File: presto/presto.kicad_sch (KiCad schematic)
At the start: 1 part

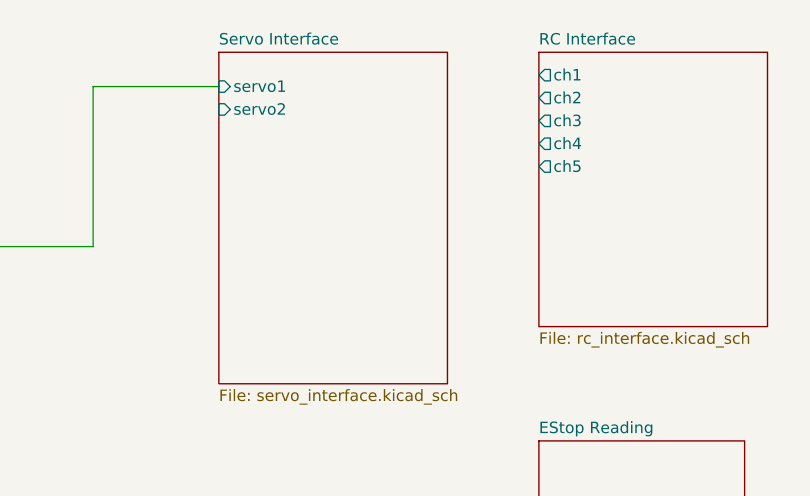
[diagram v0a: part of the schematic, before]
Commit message: RC and Servo interface schematic done
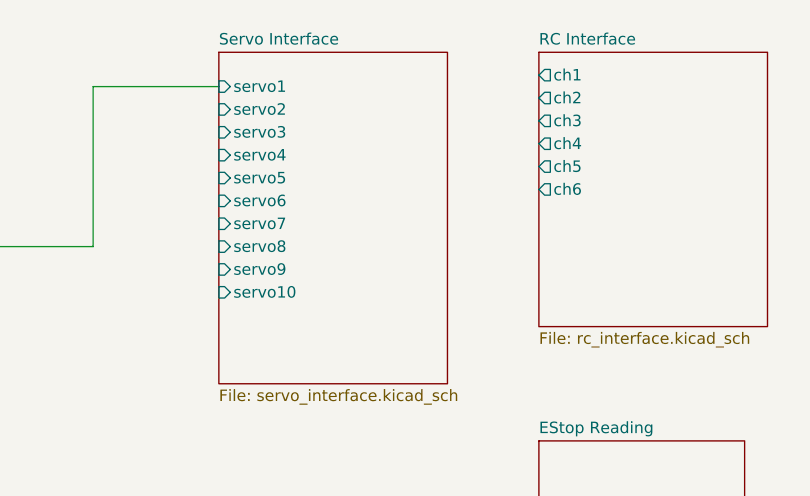
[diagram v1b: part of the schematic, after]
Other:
- sheet RC Interface ports: added ch6; removed none
- sheet Servo Interface ports: added servo10, servo3, servo4, servo5, servo6, servo7, servo8, servo9; removed none
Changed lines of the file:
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@@
+			)
+		)
+		(pin "ch6" output
+			(at 228.6 53.34 180)
+			(effects
+				(font
+					(size 1.27 1.27)
+				)
+				(justify left)
 			)
 		)
@@
 			(effects
 				(font
+					(size 1.27 1.27)
+				)
+				(justify left)
+			)
+		)
+		(pin "servo3" input
+			(at 193.04 46.99 180)
+			(effects
+				(font
+					(size 1.27 1.27)
+				)
+				(justify left)
+			)
+		)
+		(pin "servo4" input
+			(at 193.04 49.53 180)
+			(effects
+				(font
+					(size 1.27 1.27)
+				)
+				(justify left)
+			)
+		)
+		(pin "servo5" input
+			(at 193.04 52.07 180)
+			(effects
+				(font
+					(size 1.27 1.27)
+				)
+				(justify left)
+			)
+		)
+		(pin "servo6" input
+			(at 193.04 54.61 180)
+			(effects
+				(font
+					(size 1.27 1.27)
+				)
+				(justify left)
+			)
+		)
+		(pin "servo7" input
+			(at 193.04 57.15 180)
+			(effects
+				(font
+					(size 1.27 1.27)
+				)
+				(justify left)
+			)
+		)
+		(pin "servo8" input
+			(at 193.04 59.69 180)
+			(effects
+				(font
+					(size 1.27 1.27)
+				)
+				(justify left)
+			)
+		)
+		(pin "servo9" input
+			(at 193.04 62.23 180)
+			(effects
+				(font
+					(size 1.27 1.27)
+				)
+				(justify left)
+			)
+		)
+		(pin "servo10" input
+			(at 193.04 64.77 180)
+			(effects
+				(font

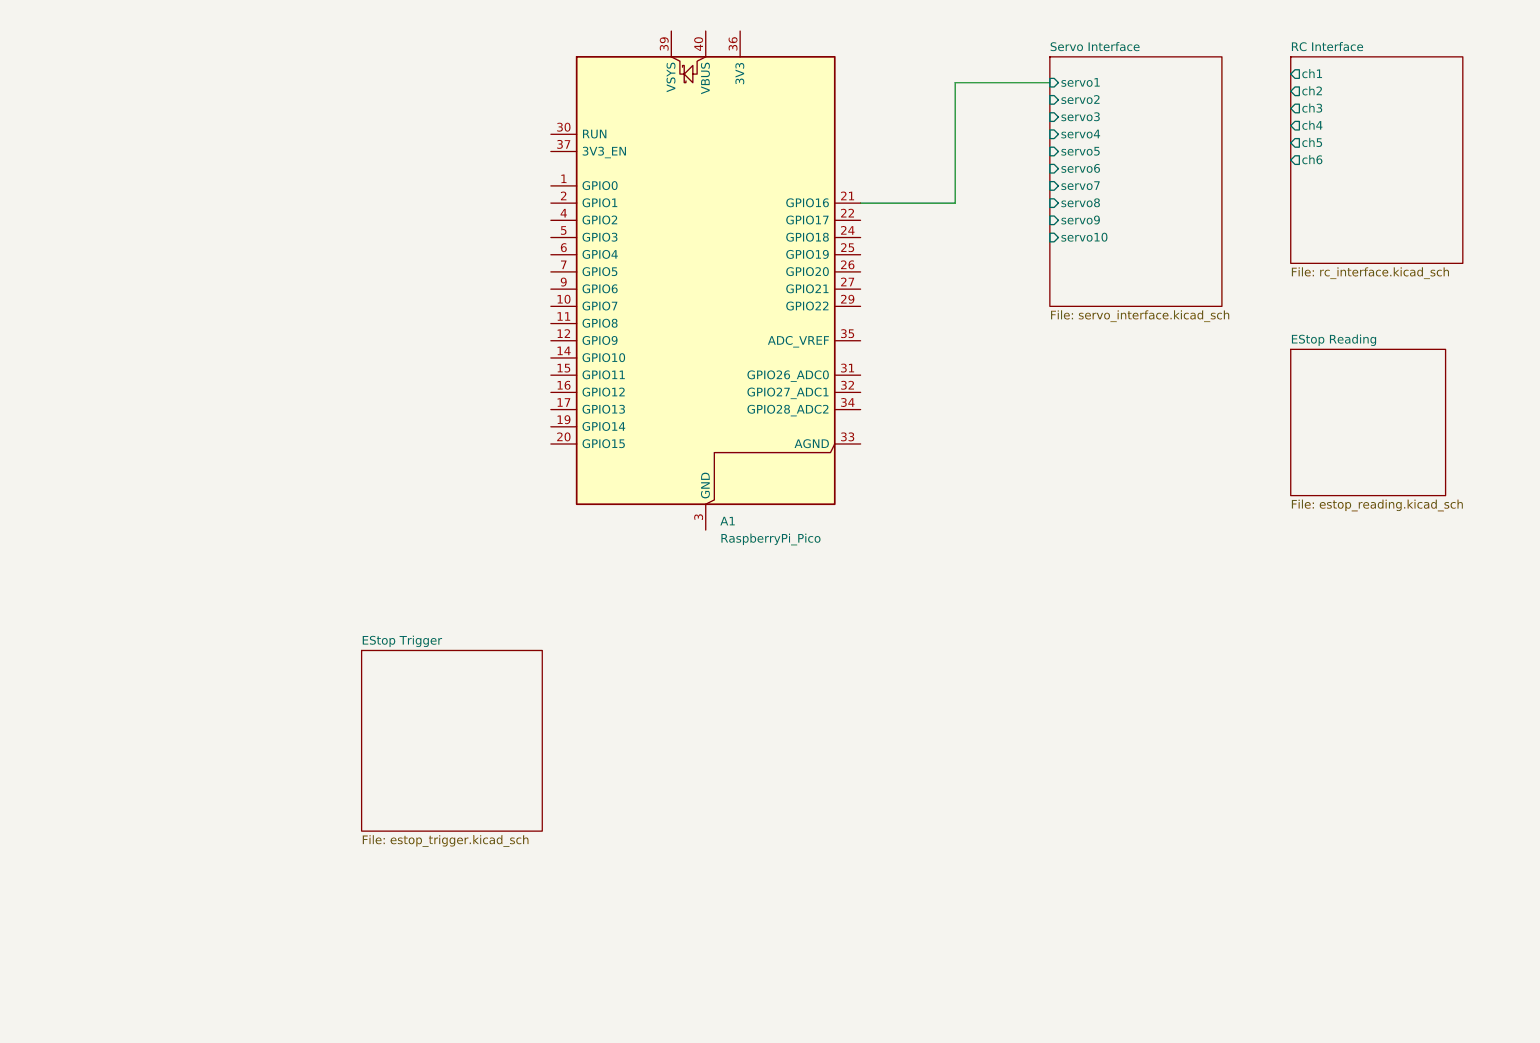
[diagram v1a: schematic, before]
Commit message: Added estop, power, led schematics
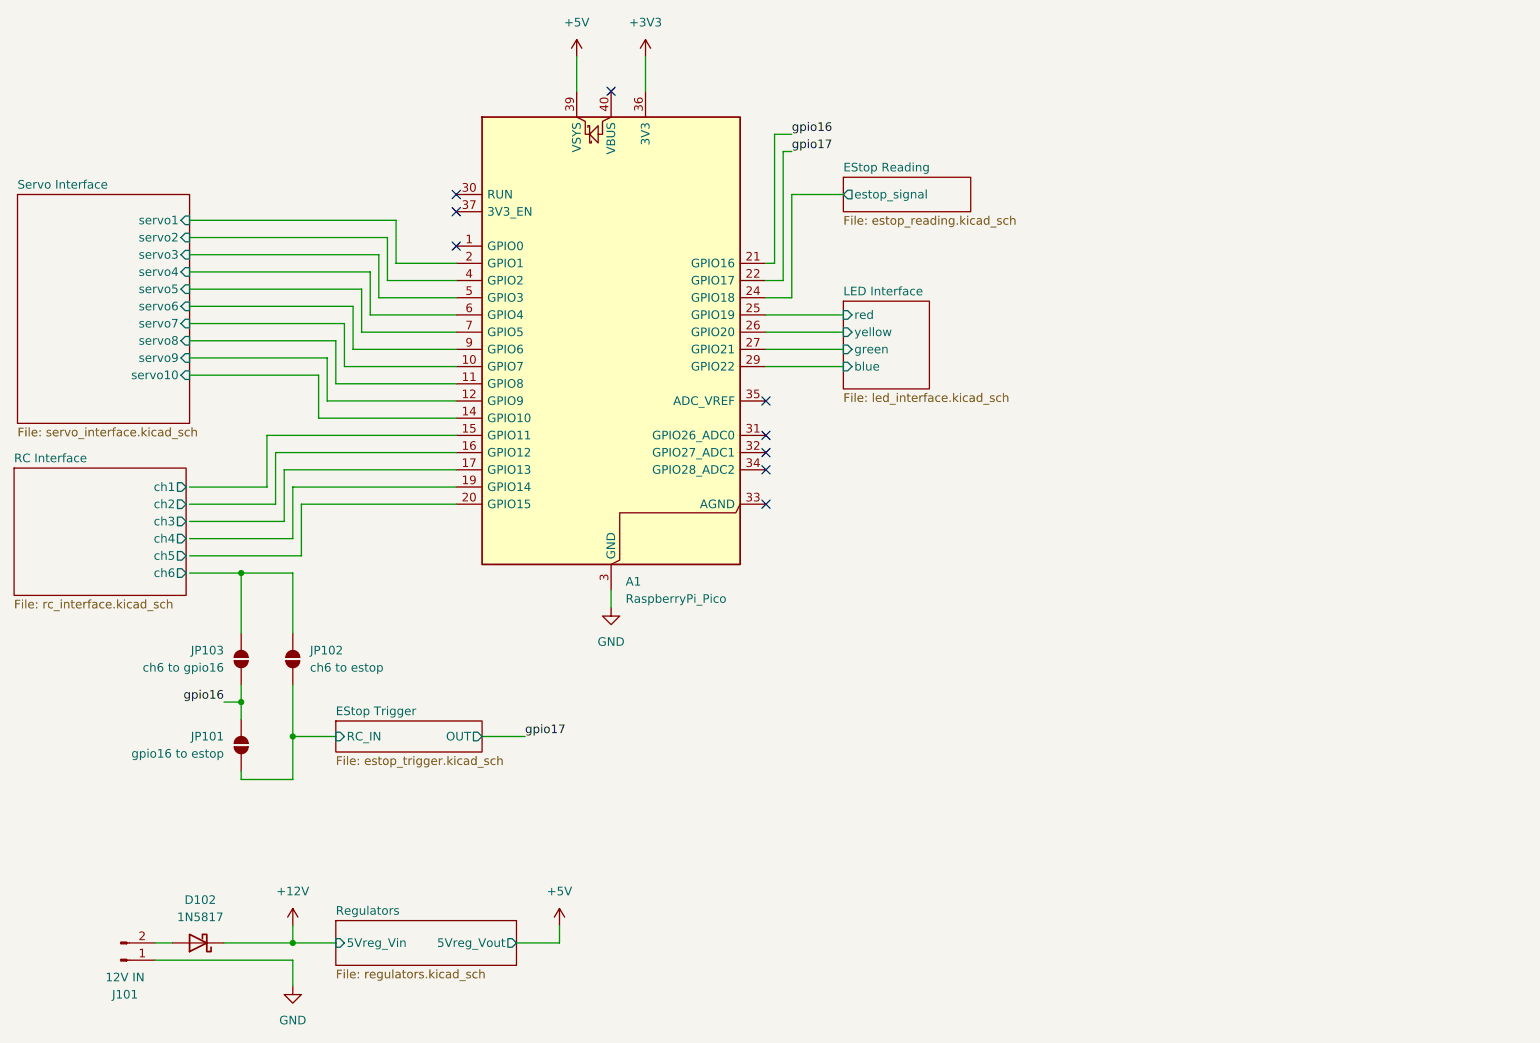
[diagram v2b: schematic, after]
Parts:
- added D102: 1N5817, Diode_THT:D_DO-41_SOD81_P10.16mm_Horizontal, symbol Diode:1N5817
- added J101: 12V IN, Connector_AMASS:AMASS_XT30PW-M_1x02_P2.50mm_Horizontal, symbol Connector:Conn_01x02_Pin
- added JP101: gpio16 to estop, Jumper:SolderJumper-2_P1.3mm_Open_RoundedPad1.0x1.5mm, symbol Jumper:SolderJumper_2_Open
- added JP102: ch6 to estop, Jumper:SolderJumper-2_P1.3mm_Open_RoundedPad1.0x1.5mm, symbol Jumper:SolderJumper_2_Open
- added JP103: ch6 to gpio16, Jumper:SolderJumper-2_P1.3mm_Open_RoundedPad1.0x1.5mm, symbol Jumper:SolderJumper_2_Open
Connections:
- net Servo Interface/servo1: now also A1.2 (GPIO1); no longer A1.21 (GPIO16)
- net Servo Interface/servo10: now also A1.14 (GPIO10)
- net Servo Interface/servo2: now also A1.4 (GPIO2)
- net Servo Interface/servo3: now also A1.5 (GPIO3)
- net Servo Interface/servo4: now also A1.6 (GPIO4)
- net Servo Interface/servo5: now also A1.7 (GPIO5)
- net Servo Interface/servo6: now also A1.9 (GPIO6)
- net Servo Interface/servo7: now also A1.10 (GPIO7)
- net Servo Interface/servo8: now also A1.11 (GPIO8)
- net Servo Interface/servo9: now also A1.12 (GPIO9)
- net GND: now reaches A1.13 (GND), A1.18 (GND), A1.23 (GND), A1.28 (GND), A1.3 (GND), A1.38 (GND), A1.8 (GND)
- net GND: now also J101.1 (Pin_1)
- net gpio17: now reaches A1.22 (GPIO17)
- net EStop Reading/estop_signal: now reaches A1.24 (GPIO18)
- net LED Interface/red: now reaches A1.25 (GPIO19)
- net LED Interface/yellow: now reaches A1.26 (GPIO20)
- net LED Interface/green: now reaches A1.27 (GPIO21)
- net LED Interface/blue: now reaches A1.29 (GPIO22)
- net +3V3: now reaches A1.36 (3V3)
- net +5V: now reaches A1.39 (VSYS)
- new net: JP102.1 (A), JP103.1 (A)
- new net: D102.2 (A), J101.2 (Pin_2)
- new net +12V: D102.1 (K)
- new net EStop Trigger/RC_IN: JP101.2 (B), JP102.2 (B)
- new net gpio16: A1.21 (GPIO16), JP101.1 (A), JP103.2 (B)
- no-connect marks 0 -> 9
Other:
- added sheet LED Interface (led_interface.kicad_sch)
- added sheet Regulators (regulators.kicad_sch)
- sheet EStop Reading ports: added estop_signal; removed none
- sheet EStop Trigger ports: added OUT, RC_IN; removed none
- moved on the sheet: A1

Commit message: Presto PCB edited with schematic, components placed, wiring in progress
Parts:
- renumbered A1 to A101, D102 to D101, JP103 to JP101, JP101 to JP102, JP102 to JP103
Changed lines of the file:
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@@
 		(on_board yes)
 		(dnp no)
-		(property "Reference" "JP102"
+		(property "Reference" "JP103"
 			(at 83.82 125.7299 90)
 			(effects
@@
 			(project ""
 				(path "/0fac30c0-3f82-4ab4-8888-b9c60b2e0ca9"
-					(reference "JP102")
+					(reference "JP103")
 					(unit 1)
 				)
@@
 		(dnp no)
 		(fields_autoplaced yes)
-		(property "Reference" "A1"
+		(property "Reference" "A101"
 			(at 130.4133 115.57 0)
 			(effects
@@
 			(project ""
 				(path "/0fac30c0-3f82-4ab4-8888-b9c60b2e0ca9"
-					(reference "A1")
+					(reference "A101")
 					(unit 1)
 				)
@@
 		(on_board yes)
 		(dnp no)
-		(property "Reference" "JP101"
+		(property "Reference" "JP102"
 			(at 71.12 138.4299 90)
 			(effects
@@
 			(project "presto"
 				(path "/0fac30c0-3f82-4ab4-8888-b9c60b2e0ca9"
-					(reference "JP101")
+					(reference "JP102")
 					(unit 1)
 				)
@@
 		(dnp no)
 		(fields_autoplaced yes)
-		(property "Reference" "#PWR0104"
+		(property "Reference" "#PWR0101"
 			(at 81.28 170.18 0)
 			(effects
@@
 			(project "presto"
 				(path "/0fac30c0-3f82-4ab4-8888-b9c60b2e0ca9"
-					(reference "#PWR0104")
+					(reference "#PWR0101")
 					(unit 1)
 				)
@@
 		(dnp no)
 		(fields_autoplaced yes)
-		(property "Reference" "D102"
+		(property "Reference" "D101"
 			(at 67.6275 162.56 0)
 			(effects
@@
 			(project ""
 				(path "/0fac30c0-3f82-4ab4-8888-b9c60b2e0ca9"
-					(reference "D102")
+					(reference "D101")
 					(unit 1)
 				)
@@
 		(dnp no)
 		(fields_autoplaced yes)
-		(property "Reference" "#PWR0102"
+		(property "Reference" "#PWR0105"
 			(at 128.27 125.73 0)
 			(effects
@@
 			(project "presto"
 				(path "/0fac30c0-3f82-4ab4-8888-b9c60b2e0ca9"
-					(reference "#PWR0102")
+					(reference "#PWR0105")
 					(unit 1)
 				)
@@
 		(dnp no)
 		(fields_autoplaced yes)
-		(property "Reference" "#PWR0103"
+		(property "Reference" "#PWR0102"
 			(at 81.28 181.61 0)
 			(effects
@@
 			(project "presto"
 				(path "/0fac30c0-3f82-4ab4-8888-b9c60b2e0ca9"
-					(reference "#PWR0103")
+					(reference "#PWR0102")
 					(unit 1)
 				)
@@
 		(dnp no)
 		(fields_autoplaced yes)
-		(property "Reference" "#PWR0106"
+		(property "Reference" "#PWR0104"
 			(at 123.19 41.91 0)
 			(effects
@@
 			(project "presto"
 				(path "/0fac30c0-3f82-4ab4-8888-b9c60b2e0ca9"
-					(reference "#PWR0106")
+					(reference "#PWR0104")
 					(unit 1)
 				)
@@
 		(dnp no)
 		(fields_autoplaced yes)
-		(property "Reference" "#PWR0101"
+		(property "Reference" "#PWR0106"
 			(at 133.35 41.91 0)
 			(effects
@@
 			(project "presto"
 				(path "/0fac30c0-3f82-4ab4-8888-b9c60b2e0ca9"
-					(reference "#PWR0101")
+					(reference "#PWR0106")
 					(unit 1)
 				)
@@
 		(dnp no)
 		(fields_autoplaced yes)
-		(property "Reference" "#PWR0105"
+		(property "Reference" "#PWR0103"
 			(at 120.65 170.18 0)
 			(effects
@@
 			(project "presto"
 				(path "/0fac30c0-3f82-4ab4-8888-b9c60b2e0ca9"
-					(reference "#PWR0105")
+					(reference "#PWR0103")
 					(unit 1)
 				)
@@
 		(on_board yes)
 		(dnp no)
-		(property "Reference" "JP103"
+		(property "Reference" "JP101"
 			(at 71.12 125.7299 90)
 			(effects
@@
 			(project "presto"
 				(path "/0fac30c0-3f82-4ab4-8888-b9c60b2e0ca9"
-					(reference "JP103")
-					(unit 1)
-				)
+					(reference "JP101")
+					(unit 1)
+				)

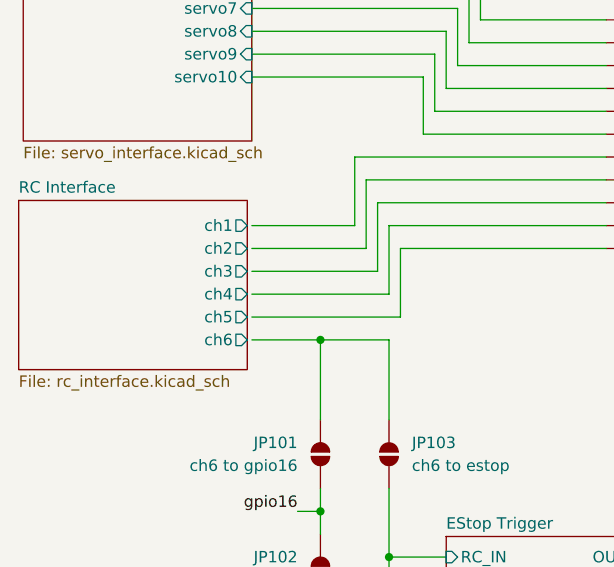
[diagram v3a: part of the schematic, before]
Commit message: Rearranged to accomodate JST
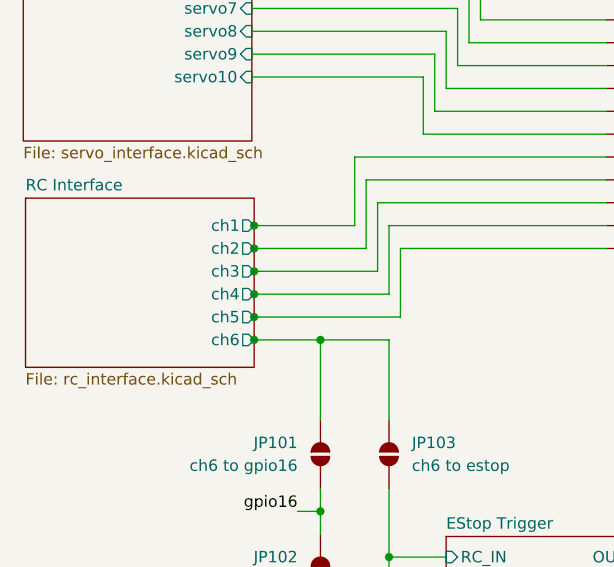
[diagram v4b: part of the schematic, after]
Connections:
- net RC Interface/ch1: now also A101.15 (GPIO11)
- net RC Interface/ch2: now also A101.16 (GPIO12)
- net RC Interface/ch3: now also A101.17 (GPIO13)
- net RC Interface/ch4: now also A101.19 (GPIO14)
- net RC Interface/ch5: now also A101.20 (GPIO15)
- net RC Interface/ch6: now also JP101.1 (A), JP103.1 (A)
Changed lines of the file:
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@@
 	(paper "A4")
+	(junction
+		(at 66.294 109.22)
+		(diameter 0)
+		(color 0 0 0 0)
+	)
+	(junction
+		(at 66.294 101.6)
+		(diameter 0)
+		(color 0 0 0 0)
+	)
+	(junction
+		(at 66.294 111.76)
+		(diameter 0)
+		(color 0 0 0 0)
+	)
+	(junction
+		(at 66.294 106.68)
+		(diameter 0)
+		(color 0 0 0 0)
+	)
 	(junction
 		(at 73.66 133.35)
@@
 	)
 	(junction
+		(at 66.294 104.14)
+		(diameter 0)
+		(color 0 0 0 0)
+	)
+	(junction
 		(at 73.66 114.3)
 		(diameter 0)
@@
 		(color 0 0 0 0)
 	)
+	(junction
+		(at 66.294 114.3)
+		(diameter 0)
+		(color 0 0 0 0)
+	)
 	(no_connect
 		(at 151.13 93.98)
@@
 	(wire
 		(pts
+			(xy 66.294 111.76) (xy 82.55 111.76)
+		)
+		(stroke
+			(width 0)
+			(type default)
+		)
+	)
+	(wire
+		(pts
 			(xy 91.44 72.39) (xy 91.44 78.74)
 		)
@@
 	(wire
 		(pts
-			(xy 66.04 106.68) (xy 80.01 106.68)
+			(xy 66.04 106.68) (xy 66.294 106.68)
+		)
+		(stroke
+			(width 0)
+			(type default)
+		)
+	)
+	(wire
+		(pts
+			(xy 66.294 101.6) (xy 77.47 101.6)
 		)
 		(stroke
@@
 	(wire
 		(pts
+			(xy 66.294 114.3) (xy 73.66 114.3)
+		)
+		(stroke
+			(width 0)
+			(type default)
+		)
+	)
+	(wire
+		(pts
 			(xy 81.28 130.81) (xy 81.28 138.43)
 		)
@@
 	(wire
 		(pts
-			(xy 66.04 101.6) (xy 77.47 101.6)
+			(xy 66.04 101.6) (xy 66.294 101.6)
 		)
 		(stroke
@@
 	(wire
 		(pts
-			(xy 66.04 109.22) (xy 81.28 109.22)
+			(xy 66.04 109.22) (xy 66.294 109.22)
 		)
 		(stroke
@@
 	(wire
 		(pts
+			(xy 66.294 109.22) (xy 81.28 109.22)
+		)
+		(stroke
+			(width 0)
+			(type default)
+		)
+	)
+	(wire
+		(pts
 			(xy 86.36 88.9) (xy 105.41 88.9)
 		)
@@
 	(wire
 		(pts
-			(xy 66.04 114.3) (xy 73.66 114.3)
-		)
-		(stroke
-			(width 0)
-			(type default)
-		)
-	)
-	(wire
-		(pts
-			(xy 66.04 104.14) (xy 78.74 104.14)
+			(xy 66.04 114.3) (xy 66.294 114.3)
+		)
+		(stroke
+			(width 0)
+			(type default)
+		)
+	)
+	(wire
+		(pts
+			(xy 66.04 104.14) (xy 66.294 104.14)
+		)
+		(stroke
+			(width 0)
+			(type default)
+		)
+	)
+	(wire
+		(pts
+			(xy 66.294 104.14) (xy 78.74 104.14)
 		)
 		(stroke
@@
 	(wire
 		(pts
+			(xy 66.294 106.68) (xy 80.01 106.68)
+		)
+		(stroke
+			(width 0)
+			(type default)
+		)
+	)
+	(wire
+		(pts
 			(xy 60.96 168.91) (xy 63.5 168.91)
 		)
@@
 	(wire
 		(pts
-			(xy 66.04 111.76) (xy 82.55 111.76)
+			(xy 66.04 111.76) (xy 66.294 111.76)
 		)
 		(stroke
@@
 	)
 	(sheet
-		(at 40.132 98.806)
+		(at 40.894 98.552)
 		(size 25.4 18.796)
 		(exclude_from_sim no)
@@
 		)
 		(property "Sheetname" "RC Interface"
-			(at 40.132 98.0944 0)
+			(at 40.894 97.8404 0)
 			(effects
 				(font
@@
 		)
 		(property "Sheetfile" "rc_interface.kicad_sch"
-			(at 40.132 118.1866 0)
+			(at 40.894 117.9326 0)
 			(effects
 				(font
@@
 		)
 		(pin "ch1" output
-			(at 65.532 101.6 0)
+			(at 66.294 101.6 0)
 			(effects
 				(font
@@
 		)
 		(pin "ch2" output
-			(at 65.532 104.14 0)
+			(at 66.294 104.14 0)
 			(effects
 				(font
@@
 		)
 		(pin "ch3" output
-			(at 65.532 106.68 0)
+			(at 66.294 106.68 0)
 			(effects
 				(font
@@
 		)
 		(pin "ch4" output
-			(at 65.532 109.22 0)
+			(at 66.294 109.22 0)
 			(effects
 				(font
@@
 		)
 		(pin "ch5" output
-			(at 65.532 111.76 0)
+			(at 66.294 111.76 0)
 			(effects
 				(font
@@
 		)
 		(pin "ch6" output
-			(at 65.532 114.3 0)
-			(effects
-				(font
+			(at 66.294 114.3 0)
+			(effects
+				(font
